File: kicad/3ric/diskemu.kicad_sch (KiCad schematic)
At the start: 4 parts

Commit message: cleaning up of the schematic
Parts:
- R1: footprint (none) -> Package_DIP:DIP-14_W7.62mm_Socket
- R2: footprint (none) -> Package_DIP:DIP-20_W7.62mm_Socket
- R3: footprint RPi_Pico:RPi_Pico_SMD_TH -> MCU_RaspberryPi_and_Boards:RPi_Pico_SMD_TH
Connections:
- no-connect marks 21 -> 23
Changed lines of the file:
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@@
 	(generator_version "8.0")
 	(paper "A4")
+	(junction
+		(at 175.26 66.04)
+		(diameter 0)
+		(color 0 0 0 0)
+	)
 	(no_connect
 		(at 143.51 171.45)
@@
 	(no_connect
 		(at 128.27 173.99)
+	)
+	(no_connect
+		(at 143.51 109.22)
+	)
+	(no_connect
+		(at 148.59 109.22)
 	)
 	(no_connect
@@
 	(wire
 		(pts
-			(xy 163.83 101.6) (xy 171.45 101.6)
+			(xy 163.83 66.04) (xy 175.26 66.04)
 		)
 		(stroke
@@
 	(wire
 		(pts
-			(xy 120.65 142.24) (xy 175.26 142.24)
+			(xy 179.07 66.04) (xy 175.26 66.04)
 		)
 		(stroke
@@
 	(wire
 		(pts
-			(xy 195.58 106.68) (xy 208.28 106.68)
+			(xy 163.83 101.6) (xy 171.45 101.6)
 		)
 		(stroke
@@
 	(wire
 		(pts
-			(xy 195.58 106.68) (xy 195.58 139.7)
+			(xy 120.65 142.24) (xy 175.26 142.24)
 		)
 		(stroke
@@
 	(wire
 		(pts
-			(xy 171.45 101.6) (xy 171.45 137.16)
+			(xy 195.58 106.68) (xy 208.28 106.68)
 		)
 		(stroke
@@
 	(wire
 		(pts
-			(xy 128.27 101.6) (xy 120.65 101.6)
+			(xy 195.58 106.68) (xy 195.58 139.7)
 		)
 		(stroke
@@
 	(wire
 		(pts
-			(xy 171.45 137.16) (xy 175.26 137.16)
+			(xy 171.45 101.6) (xy 171.45 137.16)
 		)
 		(stroke
@@
 	(wire
 		(pts
-			(xy 190.5 139.7) (xy 195.58 139.7)
+			(xy 128.27 101.6) (xy 120.65 101.6)
 		)
 		(stroke
@@
 		)
 	)
+	(wire
+		(pts
+			(xy 171.45 137.16) (xy 175.26 137.16)
+		)
+		(stroke
+			(width 0)
+			(type default)
+		)
+	)
+	(wire
+		(pts
+			(xy 190.5 139.7) (xy 195.58 139.7)
+		)
+		(stroke
+			(width 0)
+			(type default)
+		)
+	)
 	(global_label "GND"
 		(shape input)
@@
 	(global_label "P3.3"
 		(shape input)
-		(at 163.83 66.04 0)
-		(fields_autoplaced yes)
-		(effects
-			(font
-				(size 0.9906 0.9906)
-			)
-			(justify left)
-		)
-		(property "Intersheetrefs" "${INTERSHEET_REFS}"
-			(at 169.5073 66.04 0)
+		(at 179.07 66.04 0)
+		(fields_autoplaced yes)
+		(effects
+			(font
+				(size 0.9906 0.9906)
+			)
+			(justify left)
+		)
+		(property "Intersheetrefs" "${INTERSHEET_REFS}"
+			(at 184.7473 66.04 0)
 			(effects
 				(font
@@
 			)
 		)
-		(property "Footprint" ""
+		(property "Footprint" "Package_DIP:DIP-20_W7.62mm_Socket"
 			(at 220.98 93.98 0)
 			(effects
@@
 			)
 		)
-		(property "Footprint" ""
+		(property "Footprint" "Package_DIP:DIP-14_W7.62mm_Socket"
 			(at 182.88 139.7 0)
 			(effects
@@
 			)
 		)
-		(property "Footprint" ""
+		(property "Footprint" "Package_DIP:DIP-14_W7.62mm_Socket"
 			(at 135.89 171.45 0)
 			(effects
@@
 			)
 		)
-		(property "Footprint" ""
+		(property "Footprint" "Package_DIP:DIP-14_W7.62mm_Socket"
 			(at 105.41 175.26 0)
 			(effects
@@
 					(reference "R1")
 					(unit 5)
+				)
+			)
+		)
+	)
+	(symbol
+		(lib_id "power:PWR_FLAG")
+		(at 175.26 66.04 0)
+		(unit 1)
+		(exclude_from_sim no)
+		(in_bom yes)
+		(on_board yes)
+		(dnp no)
+		(fields_autoplaced yes)
+		(property "Reference" "#FLG01"
+			(at 175.26 64.135 0)
+			(effects
+				(font
+					(size 1.27 1.27)
+				)
+				(hide yes)
+			)
+		)
+		(property "Value" "PWR_FLAG"
+			(at 175.26 60.96 0)
+			(effects
+				(font
+					(size 1.27 1.27)
+				)
+			)
+		)
+		(property "Footprint" ""
+			(at 175.26 66.04 0)
+			(effects
+				(font
+					(size 1.27 1.27)
+				)
+				(hide yes)
+			)
+		)
+		(property "Datasheet" "~"
+			(at 175.26 66.04 0)
+			(effects
+				(font
+					(size 1.27 1.27)
+				)
+				(hide yes)
+			)
+		)
+		(property "Description" "Special symbol for telling ERC where power comes from"
+			(at 175.26 66.04 0)
+			(effects
+				(font
+					(size 1.27 1.27)
+				)
+				(hide yes)
+			)
+		)
+		(pin "1"
+		)
+		(instances
+			(project ""
+				(path "/e63e39d7-6ac0-4ffd-8aa3-1841a4541b55/5a1a6205-4f24-44f4-8073-12a209b744c4"
+					(reference "#FLG01")
+					(unit 1)
 				)
 			)
@@
 			)
 		)
-		(property "Footprint" ""
+		(property "Footprint" "Package_DIP:DIP-14_W7.62mm_Socket"
 			(at 156.21 186.69 0)
 			(effects
@@
 			)
 		)
-		(property "Footprint" ""
+		(property "Footprint" "Package_DIP:DIP-14_W7.62mm_Socket"
 			(at 137.16 185.42 0)
 			(effects
@@
 			)
 		)
-		(property "Footprint" "RPi_Pico:RPi_Pico_SMD_TH"
+		(property "Footprint" "MCU_RaspberryPi_and_Boards:RPi_Pico_SMD_TH"
 			(at 146.05 80.01 90)
 			(effects

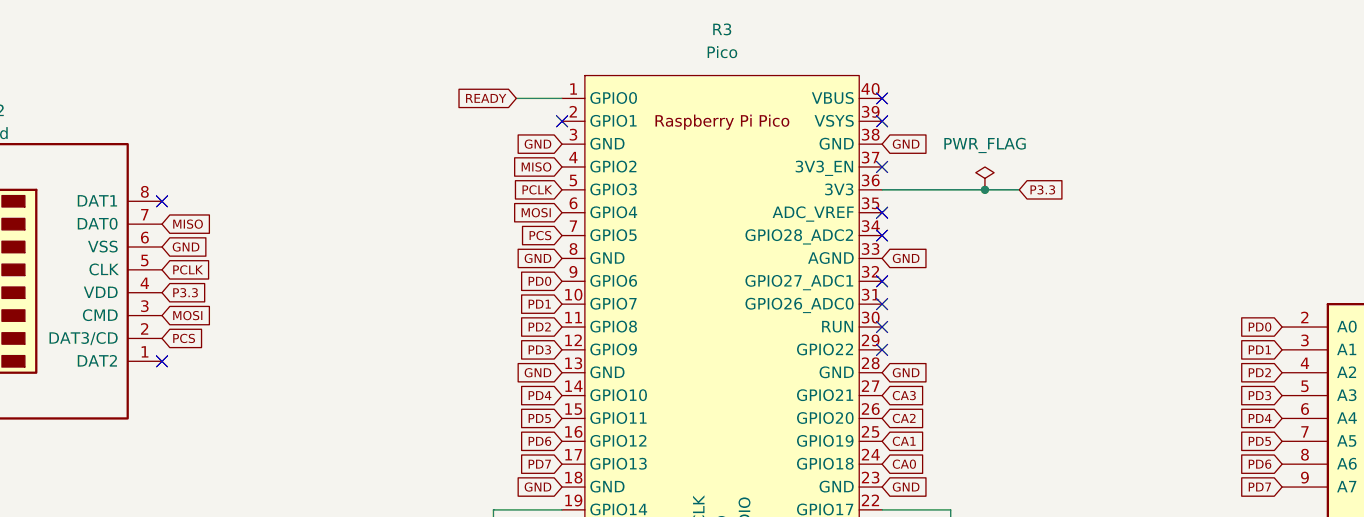
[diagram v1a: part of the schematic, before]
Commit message: updated schematics and PCB PNG of the breadboard layout
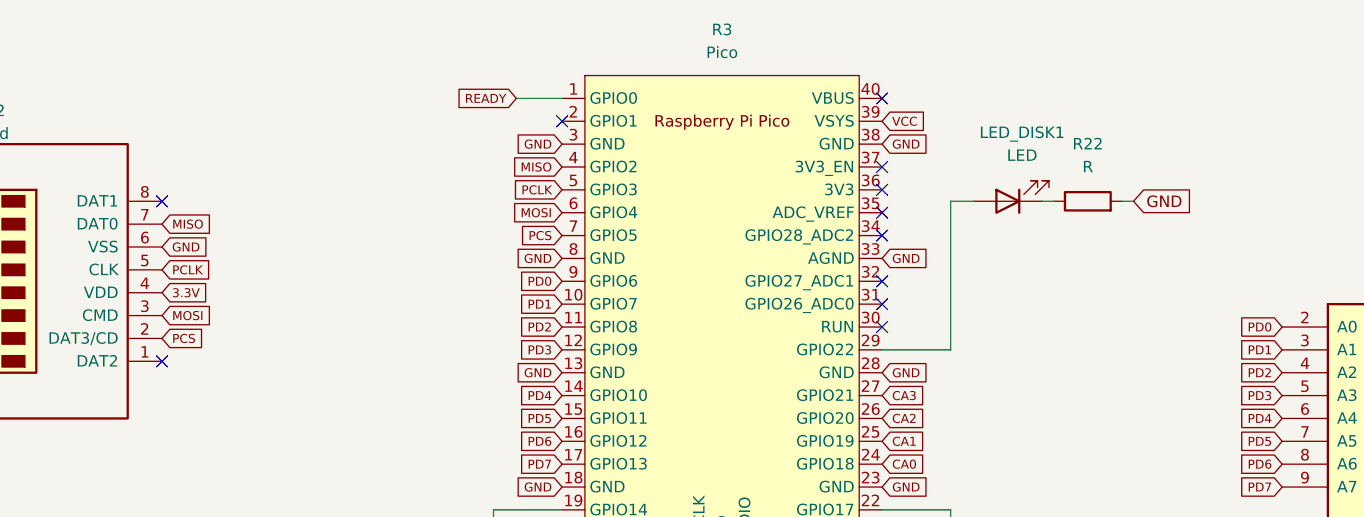
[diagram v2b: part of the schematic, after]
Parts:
- added LED_DISK1: LED, LED_THT:LED_D5.0mm, symbol Device:LED
- added R22: R, Resistor_SMD:R_0603_1608Metric_Pad0.98x0.95mm_HandSolder, symbol Device:R
- Y_MICRO_SD2: footprint badger6502pico:microSD_Amazon2 -> sdcard:microSD_Amazon2
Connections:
- net GND: now also R22.2
- net VCC: now also R3.39 (VSYS)
- net at R3.29 (GPIO22): now also LED_DISK1.2 (A)
- net P3.3: no longer names the net of R3.36 (3V3)
- net P3.3: no longer Y_MICRO_SD2.4 (VDD)
- new net: LED_DISK1.1 (K), R22.1
- new net 3.3V: Y_MICRO_SD2.4 (VDD)
- no-connect marks 23 -> 22
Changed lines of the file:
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@@
 	(generator_version "8.0")
 	(paper "A4")
-	(junction
-		(at 175.26 66.04)
-		(diameter 0)
-		(color 0 0 0 0)
-	)
 	(no_connect
 		(at 143.51 171.45)
@@
 	)
 	(no_connect
-		(at 163.83 83.82)
-	)
-	(no_connect
 		(at 163.83 68.58)
 	)
@@
 	)
 	(no_connect
+		(at 163.83 66.04)
+	)
+	(no_connect
 		(at 144.78 185.42)
 	)
@@
 	(no_connect
 		(at 163.83 76.2)
-	)
-	(no_connect
-		(at 163.83 58.42)
 	)
 	(no_connect
@@
 	(wire
 		(pts
-			(xy 163.83 66.04) (xy 175.26 66.04)
+			(xy 163.83 101.6) (xy 171.45 101.6)
 		)
 		(stroke
@@
 	(wire
 		(pts
-			(xy 179.07 66.04) (xy 175.26 66.04)
+			(xy 171.45 83.82) (xy 171.45 67.31)
 		)
 		(stroke
@@
 	(wire
 		(pts
-			(xy 163.83 101.6) (xy 171.45 101.6)
+			(xy 120.65 142.24) (xy 175.26 142.24)
 		)
 		(stroke
@@
 	(wire
 		(pts
-			(xy 120.65 142.24) (xy 175.26 142.24)
+			(xy 195.58 106.68) (xy 208.28 106.68)
 		)
 		(stroke
@@
 	(wire
 		(pts
-			(xy 195.58 106.68) (xy 208.28 106.68)
+			(xy 195.58 106.68) (xy 195.58 139.7)
 		)
 		(stroke
@@
 	(wire
 		(pts
-			(xy 195.58 106.68) (xy 195.58 139.7)
+			(xy 171.45 101.6) (xy 171.45 137.16)
 		)
 		(stroke
@@
 	(wire
 		(pts
-			(xy 171.45 101.6) (xy 171.45 137.16)
+			(xy 128.27 101.6) (xy 120.65 101.6)
 		)
 		(stroke
@@
 	(wire
 		(pts
-			(xy 128.27 101.6) (xy 120.65 101.6)
+			(xy 191.77 67.31) (xy 190.5 67.31)
 		)
 		(stroke
@@
 	(wire
 		(pts
-			(xy 171.45 137.16) (xy 175.26 137.16)
+			(xy 171.45 67.31) (xy 173.99 67.31)
 		)
 		(stroke
@@
 	(wire
 		(pts
-			(xy 190.5 139.7) (xy 195.58 139.7)
+			(xy 171.45 137.16) (xy 175.26 137.16)
 		)
 		(stroke
@@
 		)
 	)
+	(wire
+		(pts
+			(xy 163.83 83.82) (xy 171.45 83.82)
+		)
+		(stroke
+			(width 0)
+			(type default)
+		)
+	)
+	(wire
+		(pts
+			(xy 182.88 67.31) (xy 181.61 67.31)
+		)
+		(stroke
+			(width 0)
+			(type default)
+		)
+	)
+	(wire
+		(pts
+			(xy 190.5 139.7) (xy 195.58 139.7)
+		)
+		(stroke
+			(width 0)
+			(type default)
+		)
+	)
+	(global_label "VCC"
+		(shape input)
+		(at 163.83 58.42 0)
+		(fields_autoplaced yes)
+		(effects
+			(font
+				(size 0.9906 0.9906)
+			)
+			(justify left)
+		)
+		(property "Intersheetrefs" "${INTERSHEET_REFS}"
+			(at 168.9885 58.42 0)
+			(effects
+				(font
+					(size 1.27 1.27)
+				)
+				(justify left)
+				(hide yes)
+			)
+		)
+	)
 	(global_label "GND"
 		(shape input)
@@
 		)
 	)
-	(global_label "P3.3"
+	(global_label "3.3V"
 		(shape input)
 		(at 83.82 77.47 0)
@@
 		)
 		(property "Intersheetrefs" "${INTERSHEET_REFS}"
-			(at 89.4973 77.47 0)
+			(at 89.3558 77.47 0)
 			(effects
 				(font
@@
 	(global_label "GND"
 		(shape input)
+		(at 191.77 67.31 0)
+		(fields_autoplaced yes)
+		(effects
+			(font
+				(size 1.27 1.27)
+			)
+			(justify left)
+		)
+		(property "Intersheetrefs" "${INTERSHEET_REFS}"
+			(at 198.6257 67.31 0)
+			(effects
+				(font
+					(size 1.27 1.27)
+				)
+				(justify left)
+				(hide yes)
+			)
+		)
+	)
+	(global_label "GND"
+		(shape input)
 		(at 163.83 73.66 0)
 		(fields_autoplaced yes)
@@
 				)
 				(justify right)
-				(hide yes)
-			)
-		)
-	)
-	(global_label "P3.3"
-		(shape input)
-		(at 179.07 66.04 0)
-		(fields_autoplaced yes)
-		(effects
-			(font
-				(size 0.9906 0.9906)
-			)
-			(justify left)
-		)
-		(property "Intersheetrefs" "${INTERSHEET_REFS}"
-			(at 184.7473 66.04 0)
-			(effects
-				(font
-					(size 1.27 1.27)
-				)
-				(justify left)
 				(hide yes)
 			)
@@
 	)
 	(symbol
+		(lib_id "Device:R")
+		(at 186.69 67.31 90)
+		(unit 1)
+		(exclude_from_sim no)
+		(in_bom yes)
+		(on_board yes)
+		(dnp no)
+		(fields_autoplaced yes)
+		(property "Reference" "R22"
+			(at 186.69 60.96 90)
+			(effects
+				(font
+					(size 1.27 1.27)
+				)
+			)
+		)
+		(property "Value" "R"
+			(at 186.69 63.5 90)
+			(effects
+				(font
+					(size 1.27 1.27)
+				)
+			)
+		)
+		(property "Footprint" "Resistor_SMD:R_0603_1608Metric_Pad0.98x0.95mm_HandSolder"
+			(at 186.69 69.088 90)
+			(effects
+				(font
+					(size 1.27 1.27)
+				)
+				(hide yes)
+			)
+		)
+		(property "Datasheet" "~"
+			(at 186.69 67.31 0)
+			(effects
+				(font
+					(size 1.27 1.27)
+				)
+				(hide yes)
+			)
+		)
+		(property "Description" "Resistor"
+			(at 186.69 67.31 0)
+			(effects
+				(font
+					(size 1.27 1.27)
+				)
+				(hide yes)
+			)
+		)
+		(pin "2"
+		)
+		(pin "1"
+		)
+		(instances
+			(project "3ric"
+				(path "/e63e39d7-6ac0-4ffd-8aa3-1841a4541b55/5a1a6205-4f24-44f4-8073-12a209b744c4"
+					(reference "R22")
+					(unit 1)
+				)
+			)
+		)
+	)
+	(symbol
 		(lib_id "74xx:74LS08")
 		(at 182.88 139.7 0)
@@
 	)
 	(symbol
-		(lib_id "power:PWR_FLAG")
-		(at 175.26 66.04 0)
-		(unit 1)
-		(exclude_from_sim no)
-		(in_bom yes)
-		(on_board yes)
-		(dnp no)
-		(fields_autoplaced yes)
-		(property "Reference" "#FLG01"
-			(at 175.26 64.135 0)
-			(effects
-				(font
-					(size 1.27 1.27)
-				)
-				(hide yes)
-			)
-		)
-		(property "Value" "PWR_FLAG"
-			(at 175.26 60.96 0)
-			(effects
-				(font
-					(size 1.27 1.27)
-				)
-			)
-		)
-		(property "Footprint" ""
-			(at 175.26 66.04 0)
-			(effects
-				(font
-					(size 1.27 1.27)
-				)
-				(hide yes)
-			)
-		)
-		(property "Datasheet" "~"
-			(at 175.26 66.04 0)
-			(effects
-				(font
-					(size 1.27 1.27)
-				)
-				(hide yes)
-			)
-		)
-		(property "Description" "Special symbol for telling ERC where power comes from"
-			(at 175.26 66.04 0)
-			(effects
-				(font
-					(size 1.27 1.27)
-				)
-				(hide yes)
-			)
-		)
-		(pin "1"
-		)
-		(instances
-			(project ""
-				(path "/e63e39d7-6ac0-4ffd-8aa3-1841a4541b55/5a1a6205-4f24-44f4-8073-12a209b744c4"
-					(reference "#FLG01")
-					(unit 1)
-				)
-			)
-		)
-	)
-	(symbol
 		(lib_id "74xx:74LS08")
 		(at 156.21 186.69 0)
@@
 			)
 		)
-		(property "Footprint" "badger6502pico:microSD_Amazon2"
+		(property "Footprint" "sdcard:microSD_Amazon2"
 			(at 31.75 85.09 0)
 			(effects
@@
 					(unit 1)
 				)
+			)
+		)
+	)
+	(symbol
+		(lib_id "Device:LED")
+		(at 177.8 67.31 180)
+		(unit 1)
+		(exclude_from_sim no)
+		(in_bom yes)
+		(on_board yes)
+		(dnp no)
+		(fields_autoplaced yes)
+		(property "Reference" "LED_DISK1"
+			(at 179.3875 59.69 0)
+			(effects
+				(font
+					(size 1.27 1.27)
+				)
+			)
+		)
+		(property "Value" "LED"
+			(at 179.3875 62.23 0)
+			(effects
+				(font
+					(size 1.27 1.27)
+				)
+			)
+		)
+		(property "Footprint" "LED_THT:LED_D5.0mm"
+			(at 177.8 67.31 0)
+			(effects
+				(font
+					(size 1.27 1.27)
+				)
+				(hide yes)
+			)
+		)
+		(property "Datasheet" "~"
+			(at 177.8 67.31 0)
+			(effects
+				(font
+					(size 1.27 1.27)
+				)
+				(hide yes)
+			)
+		)
+		(property "Description" "Light emitting diode"
+			(at 177.8 67.31 0)
+			(effects
+				(font
+					(size 1.27 1.27)
+				)
+				(hide yes)
+			)
+		)
+		(pin "1"
+		)
+		(pin "2"
+		)
+		(instances
+			(project "3ric"
+				(path "/e63e39d7-6ac0-4ffd-8aa3-1841a4541b55/5a1a6205-4f24-44f4-8073-12a209b744c4"
+					(reference "LED_DISK1")
+					(unit 1)
+				)

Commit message: pcb layout continued
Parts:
- removed LED_DISK1: LED, LED_THT:LED_D5.0mm, symbol Device:LED
- added J7: Conn_01x02_Pin, Connector_PinHeader_2.54mm:PinHeader_2x01_P2.54mm_Vertical, symbol Connector:Conn_01x02_Pin
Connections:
- net MISO: now also R3.6 (GPIO4); no longer R3.4 (GPIO2)
- net MOSI: now also R3.5 (GPIO3); no longer R3.6 (GPIO4)
- net PCLK: now also R3.4 (GPIO2); no longer R3.5 (GPIO3)
- net at R22.1: now also J7.1 (Pin_1)
- net at R3.29 (GPIO22): now also J7.2 (Pin_2)
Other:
- moved on the sheet: R22

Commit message: so close!  PCB ready to go?
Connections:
- net at R1.1: now also R3.19 (GPIO14); no longer R3.22 (GPIO17)
- net at R1.2: now also R3.22 (GPIO17); no longer R3.19 (GPIO14)
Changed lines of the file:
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@@
 		(lib_id "74xx:74LS08")
 		(at 182.88 139.7 0)
+		(mirror x)
 		(unit 1)
 		(exclude_from_sim no)
@@
 		(on_board yes)
 		(dnp no)
-		(fields_autoplaced yes)
 		(property "Reference" "R1"
-			(at 182.8717 130.81 0)
+			(at 182.8717 148.59 0)
 			(effects
 				(font
@@
 		)
 		(property "Value" "74LS08"
-			(at 182.8717 133.35 0)
+			(at 182.8717 146.05 0)
 			(effects
 				(font

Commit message: v2 pcb
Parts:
- removed R1: 74LS08, Package_DIP:DIP-14_W7.62mm_Socket, symbol 74xx:74LS08
- added A5: 74LS08, Package_DIP:DIP-14_W7.62mm_Socket, symbol 74xx:74LS08
- R22: value R -> R220
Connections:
- net at R2.19 (CE): now also A5.11
- net DISKSS: now reaches R3.19 (GPIO14)
- net DISKSS: now also A5.13
- net C7XX: now reaches R3.22 (GPIO17)
- net C7XX: now also A5.12
- no-connect marks 22 -> 13
